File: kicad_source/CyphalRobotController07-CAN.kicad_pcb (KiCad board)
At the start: 2 copper layers, 140 x 70 mm, 161 parts, among them J1 BM04B-SRSS-TB, J10 x, J11 PowerPole, J12 Conn_01x02, J13 Conn_01x02, J14 Conn_01x02, J15 PinHeader_1x04, J16 PinHeader_1x04, J17 PinHeader_1x05, J2 RASPBERRYPI_PICO, J3 BM04B-SRSS-TB, J4 B3B-PH-SM4-TB, J5 BM04B-GHS-TBT, J6 BM04B-GHS-TBT, J7 x, J8 x, J9 x, Q1 2N7002, Q2 IPD90P03P4L- 04, SW1 PTS636 SM43 SMTR LFS, U1 24LC64-I/SN, U10 ADS1015IDGS, U11 OPA2374AIDCN, U12 INA226, U13 IFX91041EFJ, U14 ITS4200S-ME-P, U15 ITS4200S-ME-P, U16 BNO085, U2 MCP2515-I/SO, U3 SN65HVD232, U4 74xx08, U5 IFX007T, U6 IFX007T, U7 IFX007T, U8 IFX007T, U9 OPA2374AIDCN, Y1 RH100-16.000-16-3030-EXT-TR, Y2 DNI

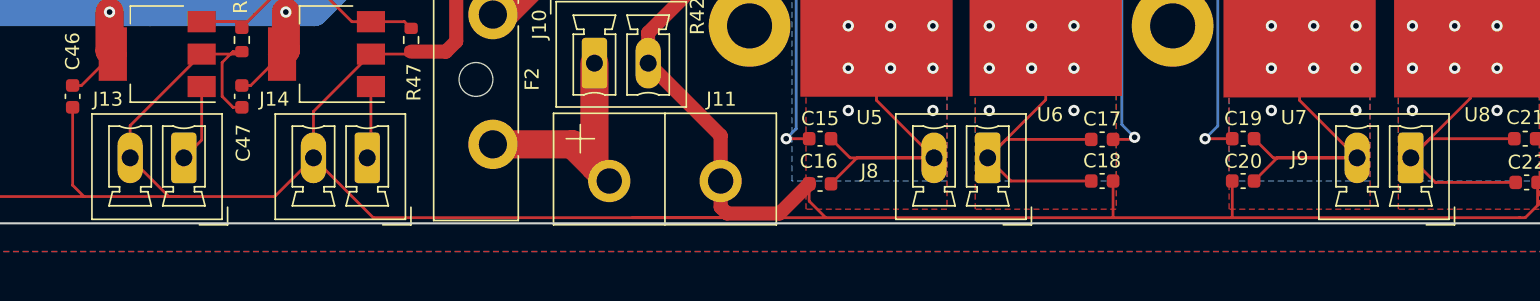
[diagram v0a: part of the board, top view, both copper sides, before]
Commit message: updated 3d model to fit to reality
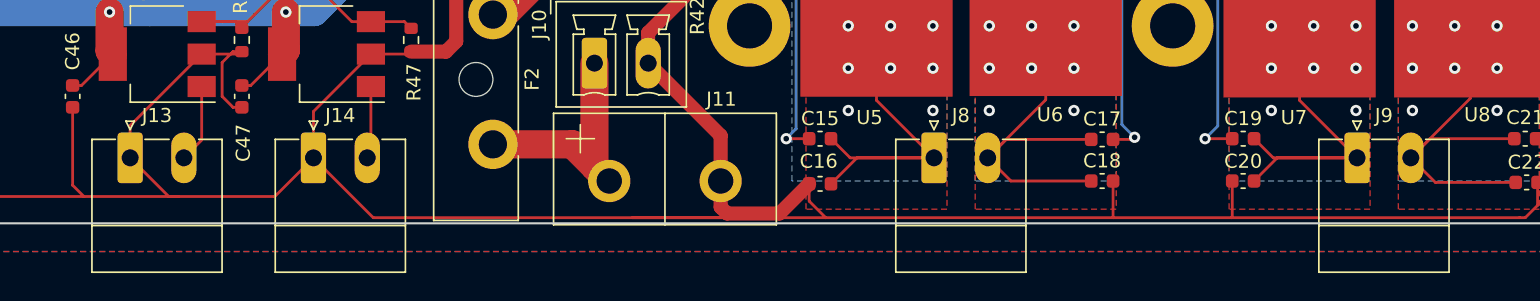
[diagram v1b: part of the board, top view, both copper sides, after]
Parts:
- C46, C47: value C_Small -> 100 nF
- F2: footprint Fuse:Fuseholder_Blade_ATO_Littelfuse_Pudenz_2_Pin -> generationmake:Fuseholder_Blade_ATO_Littelfuse_Pudenz_2_Pin
- J13, J14, J8, J9: footprint Connector_Phoenix_MC:PhoenixContact_MCV_1,5_2-G-3.81_1x02_P3.81mm_Vertical -> Connector_Phoenix_MC:PhoenixContact_MC_1,5_2-G-3.81_1x02_P3.81mm_Horizontal
- R28, R54: value DNI -> 0R
- R46, R47: value R_Small -> 10k
- moved J13 3.81 mm to (83.1, 121.4), turned to 0 degrees
- moved J14 3.81 mm to (96.1, 121.4), turned to 0 degrees
- moved J8 3.81 mm to (140.1, 121.4), turned to 0 degrees
- moved J9 3.81 mm to (170.1, 121.4), turned to 0 degrees
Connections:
- J13 pad 1: /inout_output/OUT0 -> GND
- J13 pad 2: GND -> /inout_output/OUT0
- J14 pad 1: /inout_output/OUT1 -> GND
- J14 pad 2: GND -> /inout_output/OUT1
- J8 pad 1: OUT2 -> OUT1
- J8 pad 2: OUT1 -> OUT2
- J9 pad 1: OUT4 -> OUT3
- J9 pad 2: OUT3 -> OUT4

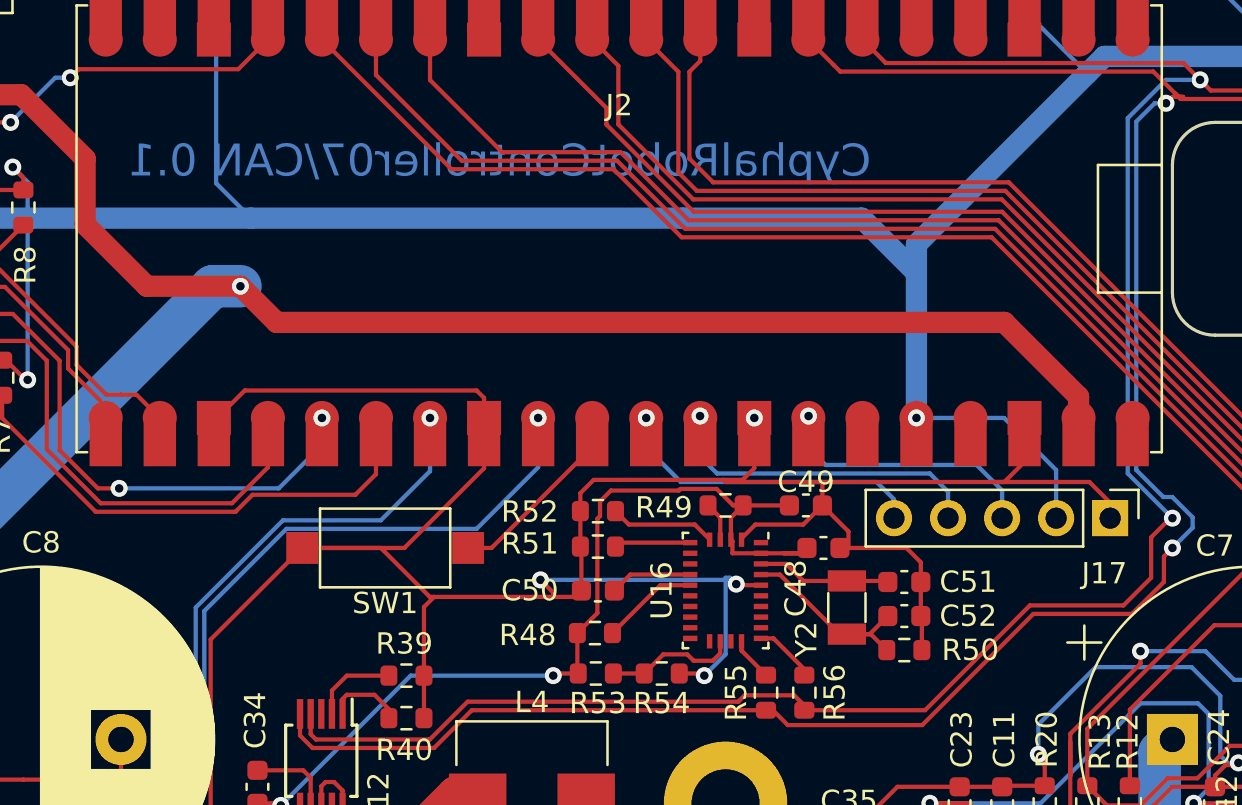
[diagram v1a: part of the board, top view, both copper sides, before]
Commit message: combined 3.3V nets
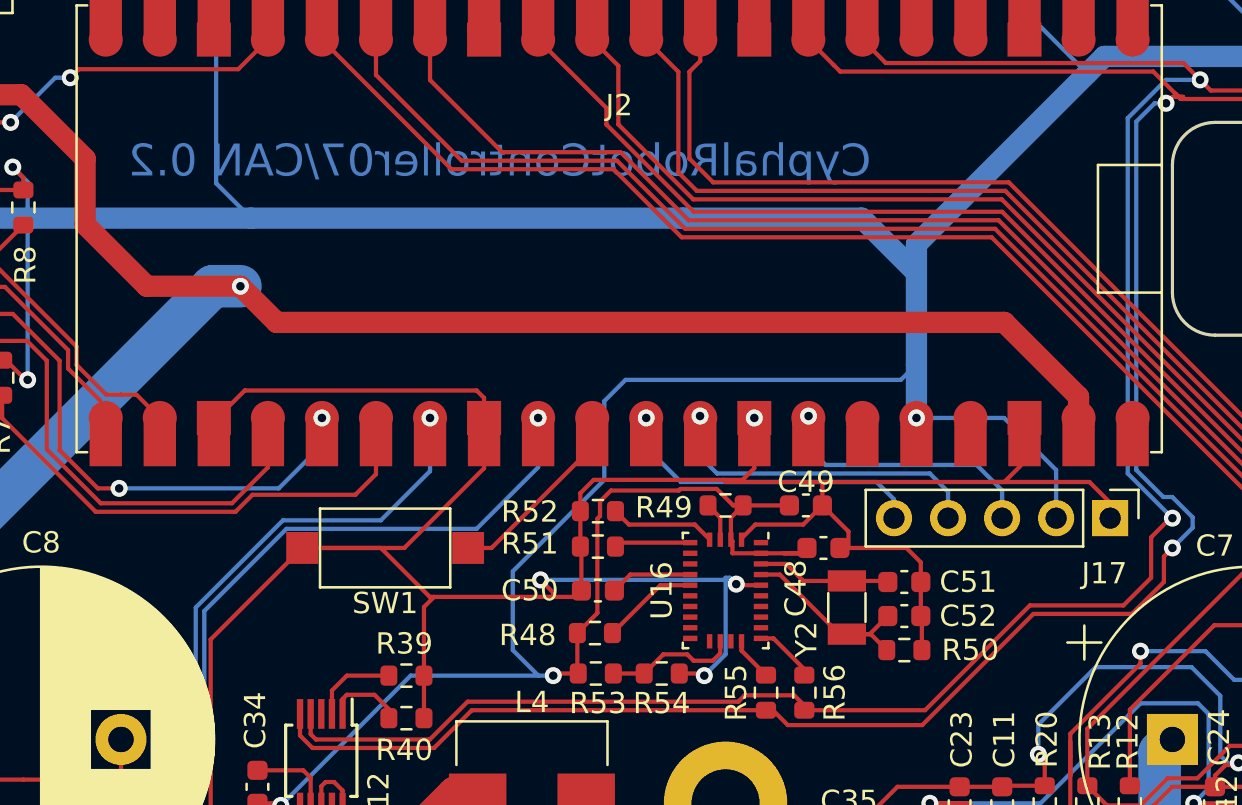
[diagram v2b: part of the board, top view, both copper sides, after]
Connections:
- C34 pad 1: +3V3 -> +3.3V
- C48 pad 1: +3V3 -> +3.3V
- C49 pad 1: +3V3 -> +3.3V
- R48 pad 1: +3V3 -> +3.3V
- R49 pad 1: +3V3 -> +3.3V
- R53 pad 1: +3V3 -> +3.3V
- U12 pad 6: +3V3 -> +3.3V
- U16 pad 28: +3V3 -> +3.3V
- U16 pad 3: +3V3 -> +3.3V
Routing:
- net +3.3V: track 307.3 -> 384.0 mm, vias 11 -> 13
- net +3V3: track 46.2 -> 0.00 mm, vias 2 -> 0
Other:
- board text added: "CyphalRobotController07/CAN 0.2"
- board text removed: "CyphalRobotController07/CAN 0.1"

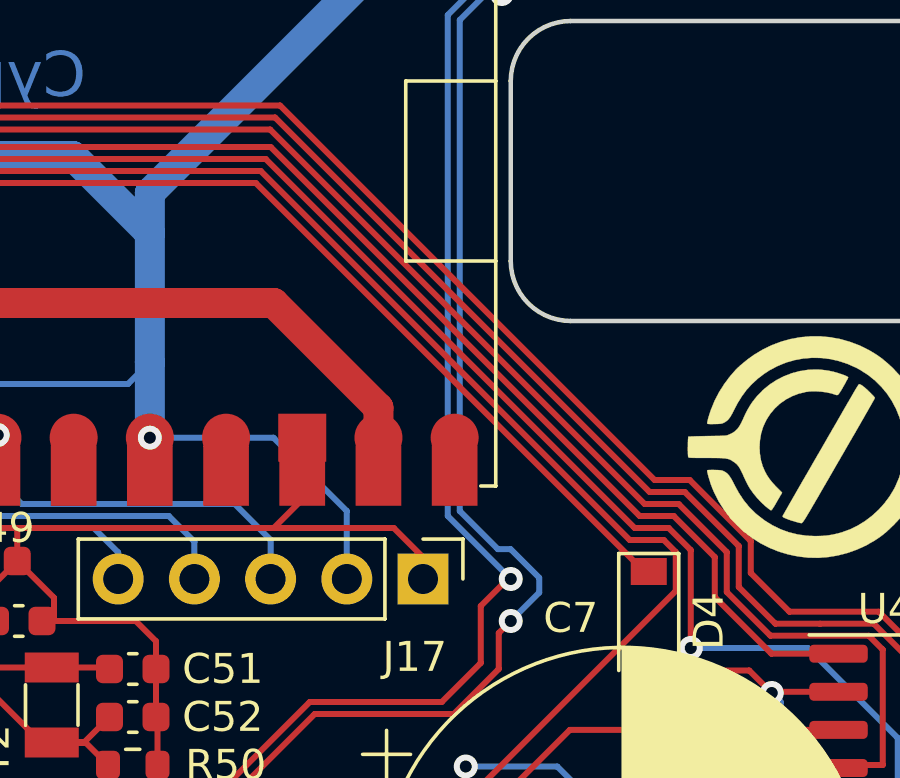
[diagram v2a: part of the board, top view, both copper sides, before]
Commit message: added weak pull down on EM_STOP_D
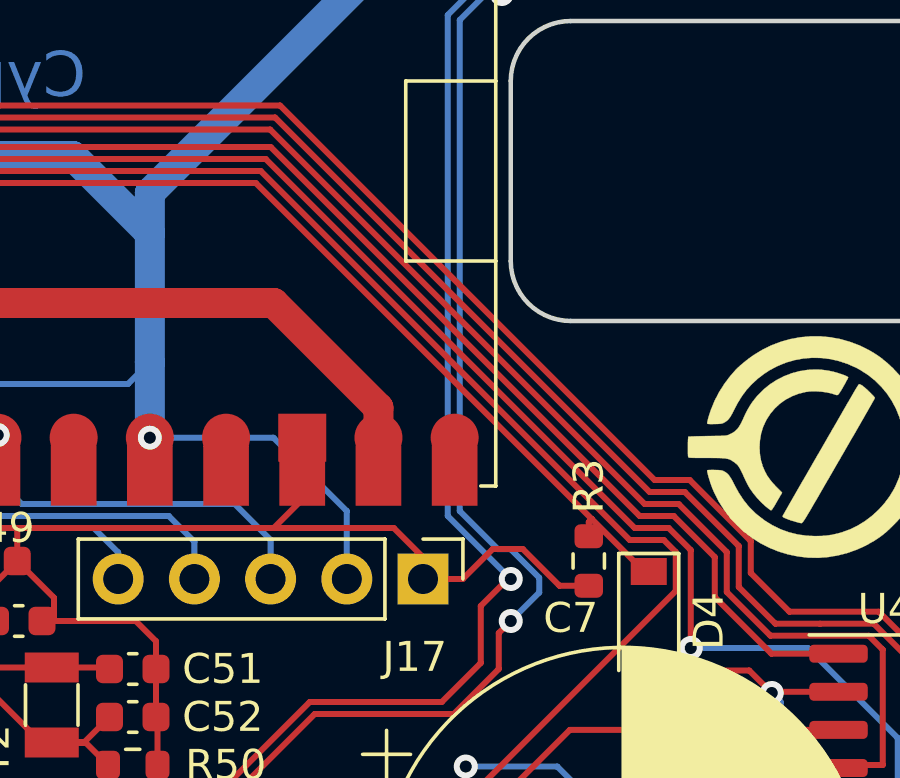
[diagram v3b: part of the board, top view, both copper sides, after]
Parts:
- added R3: 100k, Resistor_SMD:R_0603_1608Metric, F.Cu at (144.6, 85.0)
- R45: value 2k2 -> 1k3
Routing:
- net GND: track 1015.6 -> 1022.0 mm
- net EM_STOP_D: track 53.8 -> 54.4 mm
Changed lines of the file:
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@@
       (effects (font (size 1 1) (thickness 0.15)))
     )
-    (fp_text value "2k2" (at 0 1.43 90) (layer "F.Fab")
+    (fp_text value "1k3" (at 0 1.43 90) (layer "F.Fab")
       (effects (font (size 1 1) (thickness 0.15)))
     )
@@
   )
   (footprint "Resistor_SMD:R_0603_1608Metric" (layer "F.Cu")
+    (at 144.6 85 -90)
+    (descr "Resistor SMD 0603 (1608 Metric), square (rectangular) end terminal, IPC_7351 nominal, (Body size source: IPC-SM-782 page 72, https://www.pcb-3d.com/wordpress/wp-content/uploads/ipc-sm-782a_amendment_1_and_2.pdf), generated with kicad-footprint-generator")
+    (tags "resistor")
+    (property "Sheetfile" "MotorDriver.kicad_sch")
+    (property "Sheetname" "MotorDriver")
+    (attr smd)
+    (fp_text reference "R3" (at -2.5 0 90) (layer "F.SilkS")
+      (effects (font (size 1 1) (thickness 0.15)))
+    )
+    (fp_text value "100k" (at 0 1.43 90) (layer "F.Fab")
+      (effects (font (size 1 1) (thickness 0.15)))
+    )
+    (fp_text user "${REFERENCE}" (at 0 0 90) (layer "F.Fab")
+      (effects (font (size 0.4 0.4) (thickness 0.06)))
+    )
+    (fp_line (start -0.237258 -0.5225) (end 0.237258 -0.5225) (layer "F.SilkS") (width 0.12))
+    (fp_line (start -0.237258 0.5225) (end 0.237258 0.5225) (layer "F.SilkS") (width 0.12))
+    (fp_line (start -1.48 -0.73) (end 1.48 -0.73) (layer "F.CrtYd") (width 0.05))
+    (fp_line (start 1.48 -0.73) (end 1.48 0.73) (layer "F.CrtYd") (width 0.05))
+    (fp_line (start 1.48 0.73) (end -1.48 0.73) (layer "F.CrtYd") (width 0.05))
+    (fp_line (start -1.48 0.73) (end -1.48 -0.73) (layer "F.CrtYd") (width 0.05))
+    (fp_line (start 0.8 0.4125) (end -0.8 0.4125) (layer "F.Fab") (width 0.1))
+    (fp_line (start -0.8 -0.4125) (end 0.8 -0.4125) (layer "F.Fab") (width 0.1))
+    (fp_line (start 0.8 -0.4125) (end 0.8 0.4125) (layer "F.Fab") (width 0.1))
+    (fp_line (start -0.8 0.4125) (end -0.8 -0.4125) (layer "F.Fab") (width 0.1))
+    (pad "1" smd roundrect (at -0.825 0 270) (size 0.8 0.95) (layers "F.Cu" "F.Paste" "F.Mask") (roundrect_rratio 0.25)
+      (net 77 "EM_STOP_D") (pintype "passive"))
+    (pad "2" smd roundrect (at 0.825 0 270) (size 0.8 0.95) (layers "F.Cu" "F.Paste" "F.Mask") (roundrect_rratio 0.25)
+      (net 1 "GND") (pintype "passive"))
+    (model "${KICAD6_3DMODEL_DIR}/Resistor_SMD.3dshapes/R_0603_1608Metric.wrl"
+      (offset (xyz 0 0 0))
+      (scale (xyz 1 1 1))
+      (rotate (xyz 0 0 0))
+    )
+  )
+  (footprint "Resistor_SMD:R_0603_1608Metric" (layer "F.Cu")
     (at 176 93 180)
     (descr "Resistor SMD 0603 (1608 Metric), square (rectangular) end terminal, IPC_7351 nominal, (Body size source: IPC-SM-782 page 72, https://www.pcb-3d.com/wordpress/wp-content/uploads/ipc-sm-782a_amendment_1_and_2.pdf), generated with kicad-footprint-generator")
@@
   (segment (start 183.3 81.1) (end 182.925 81.475) (width 0.2) (layer "F.Cu") (net 1))
   (segment (start 69 88.8875) (end 74 88.8875) (width 0.2) (layer "F.Cu") (net 1))
+  (segment (start 144.6 85.825) (end 143.625 85.825) (width 0.2) (layer "F.Cu") (net 1))
   (segment (start 132 98.225) (end 129.075 98.225) (width 0.2) (layer "F.Cu") (net 1))
   (segment (start 154.4625 103.125) (end 151.81 103.125) (width 0.2) (layer "F.Cu") (net 1))
@@
   (segment (start 139.075 85.6) (end 139.075 84.875) (width 0.2) (layer "F.Cu") (net 1))
   (segment (start 102.825 114) (end 103 113.825) (width 0.2) (layer "F.Cu") (net 1))
+  (segment (start 141.4 84.6) (end 140.4 85.6) (width 0.2) (layer "F.Cu") (net 1))
   (segment (start 58.2 93) (end 60.25 90.95) (width 0.2) (layer "F.Cu") (net 1))
   (segment (start 53.5 104.4) (end 52.8 103.7) (width 0.2) (layer "F.Cu") (net 1))
@@
   (segment (start 130.175 88.6) (end 130.175 87.675) (width 0.2) (layer "F.Cu") (net 1))
   (segment (start 77.5 61.5) (end 78.1 61.5) (width 0.2) (layer "F.Cu") (net 1))
+  (segment (start 140.4 85.6) (end 139.075 85.6) (width 0.2) (layer "F.Cu") (net 1))
   (segment (start 60.25 89.55) (end 60.8 89) (width 0.2) (layer "F.Cu") (net 1))
   (segment (start 169.225 77) (end 169.225 77.925) (width 0.2) (layer "F.Cu") (net 1))
@@
   (segment (start 165 83.725) (end 165.82 82.905) (width 0.2) (layer "F.Cu") (net 1))
   (segment (start 75.6 63.8) (end 77.5 61.9) (width 0.2) (layer "F.Cu") (net 1))
+  (segment (start 142.4 84.6) (end 141.4 84.6) (width 0.2) (layer "F.Cu") (net 1))
   (segment (start 79.25625 94.14375) (end 74 88.8875) (width 0.2) (layer "F.Cu") (net 1))
   (segment (start 180.7 66.5) (end 178.6 64.4) (width 0.2) (layer "F.Cu") (net 1))
@@
   (segment (start 66.3 124.3) (end 66.5 124.3) (width 0.2) (layer "F.Cu") (net 1))
   (segment (start 162.015 98.225) (end 161.99 98.2) (width 0.2) (layer "F.Cu") (net 1))
+  (segment (start 143.625 85.825) (end 142.4 84.6) (width 0.2) (layer "F.Cu") (net 1))
   (segment (start 86.5 124.1) (end 85.82 124.1) (width 0.2) (layer "F.Cu") (net 1))
   (segment (start 114.175 85.27) (end 114.175 84.425) (width 0.2) (layer "F.Cu") (net 1))
@@
   (segment (start 63.32 122.505) (end 62.825 123) (width 0.2) (layer "F.Cu") (net 76))
   (segment (start 65 122.505) (end 63.32 122.505) (width 0.2) (layer "F.Cu") (net 76))
-  (segment (start 133.5 72.4) (end 146.45 85.35) (width 0.2) (layer "F.Cu") (net 77))
+  (segment (start 144.6 83.7) (end 144.7 83.6) (width 0.2) (layer "F.Cu") (net 77))
   (segment (start 115.734314 69.2) (end 118.934315 72.4) (width 0.2) (layer "F.Cu") (net 77))
+  (segment (start 144.7 83.6) (end 146.45 85.35) (width 0.2) (layer "F.Cu") (net 77))
   (segment (start 108.12 69.2) (end 115.734314 69.2) (width 0.2) (layer "F.Cu") (net 77))
+  (segment (start 133.5 72.4) (end 144.7 83.6) (width 0.2) (layer "F.Cu") (net 77))
   (segment (start 102.03 63.11) (end 108.12 69.2) (width 0.2) (layer "F.Cu") (net 77))
+  (segment (start 144.6 84.175) (end 144.6 83.7) (width 0.2) (layer "F.Cu") (net 77))
   (segment (start 118.934315 72.4) (end 133.5 72.4) (width 0.2) (layer "F.Cu") (net 77))
   (segment (start 146.45 85.35) (end 146.6 85.35) (width 0.2) (layer "F.Cu") (net 77))

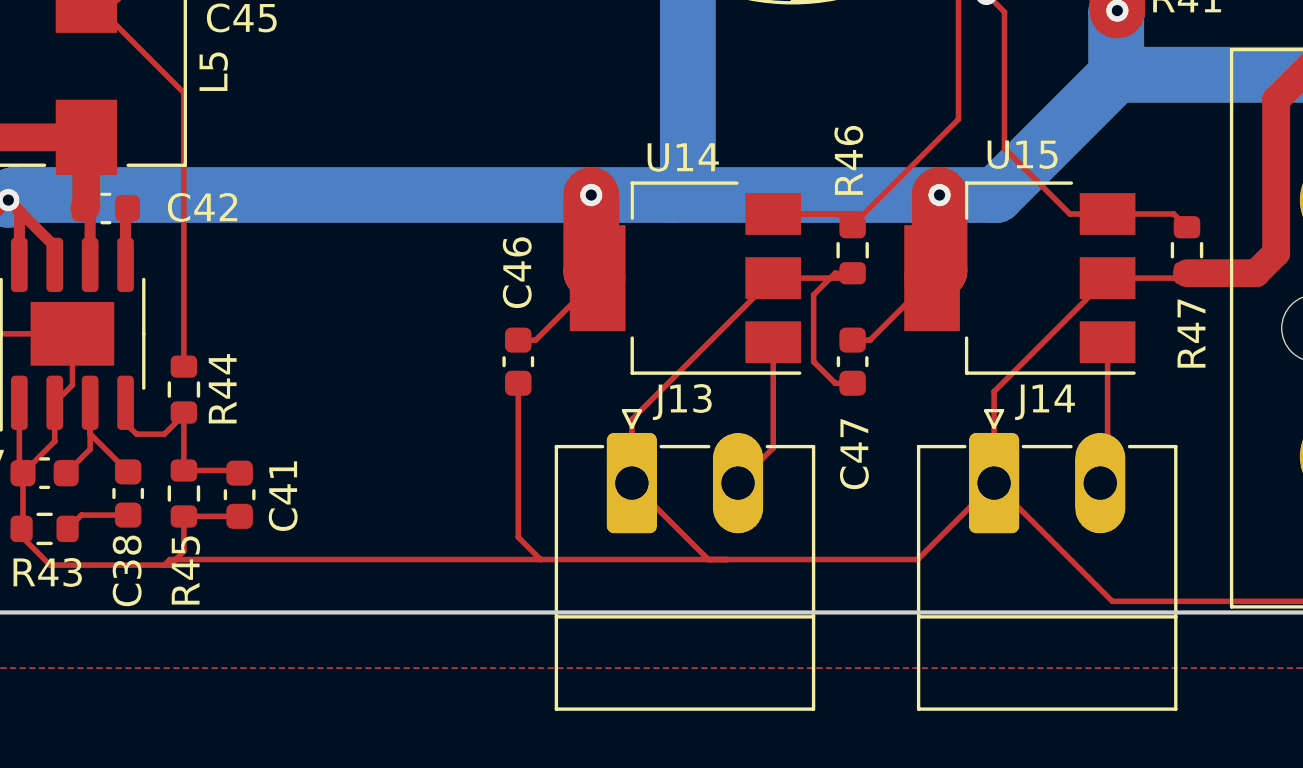
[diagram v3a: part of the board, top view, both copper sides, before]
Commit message: added always on connector for +BATT
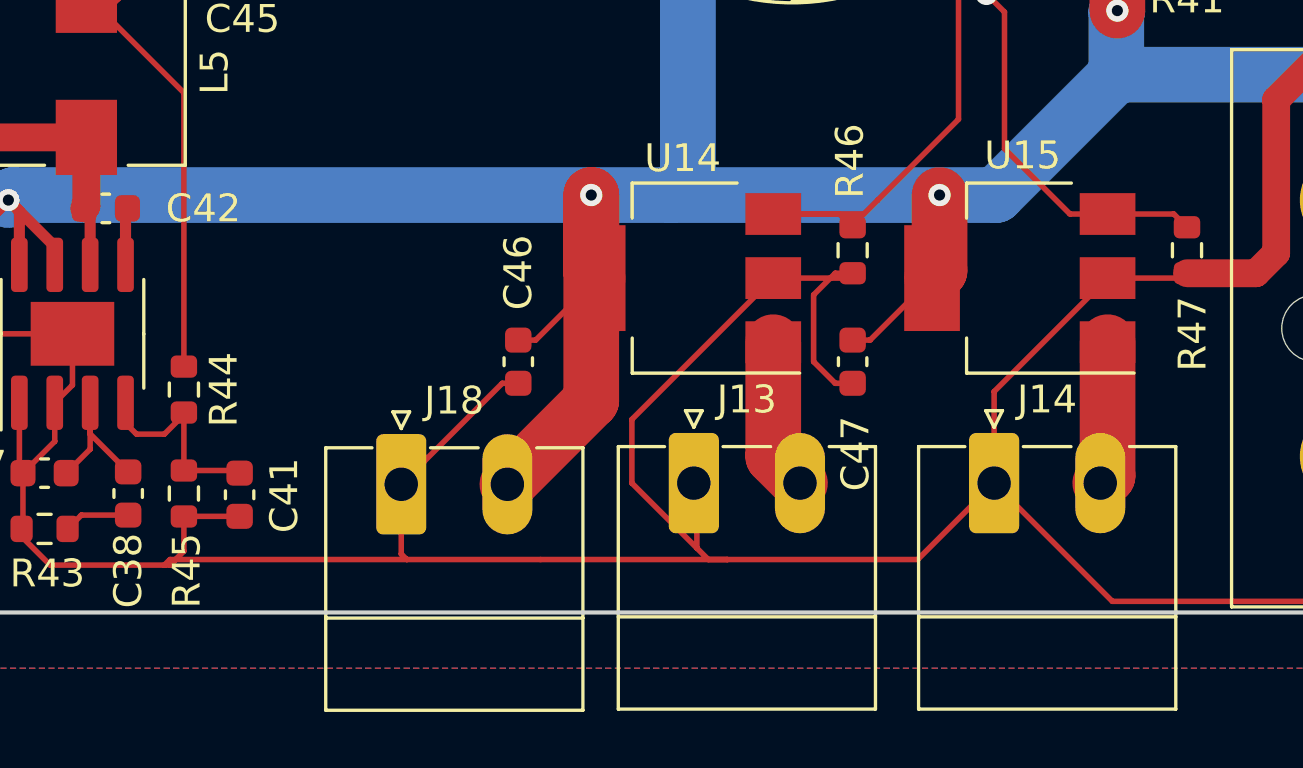
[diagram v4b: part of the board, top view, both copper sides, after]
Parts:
- added J18: Conn_01x02, Connector_Phoenix_MC:PhoenixContact_MC_1,5_2-G-3.81_1x02_P3.81mm_Horizontal, F.Cu at (74.8, 121.4)
- moved J13 2.22 mm to (85.3, 121.4)
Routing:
- net +BATT: track 310.5 -> 322.2 mm
- net GND: track 1022.0 -> 1026.2 mm
